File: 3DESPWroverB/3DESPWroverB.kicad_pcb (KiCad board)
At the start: 2 copper layers, 92.2 x 40 mm, 18 parts, among them J1 Conn_02x07_Odd_Even, J10 Conn_02x03_Odd_Even, J11 Conn_01x01, J12 Conn_01x01, J13 Conn_01x01, J14 Conn_01x01, J15 Conn_01x01, J16 Conn_01x01, J17 Conn_01x01, J18 Conn_01x01, J2 Conn_01x01, J3 Conn_01x01, J4 Conn_01x01, J5 Conn_01x01, J6 Conn_01x01, J7 Conn_01x01, J8 Conn_01x01, J9 Conn_01x01

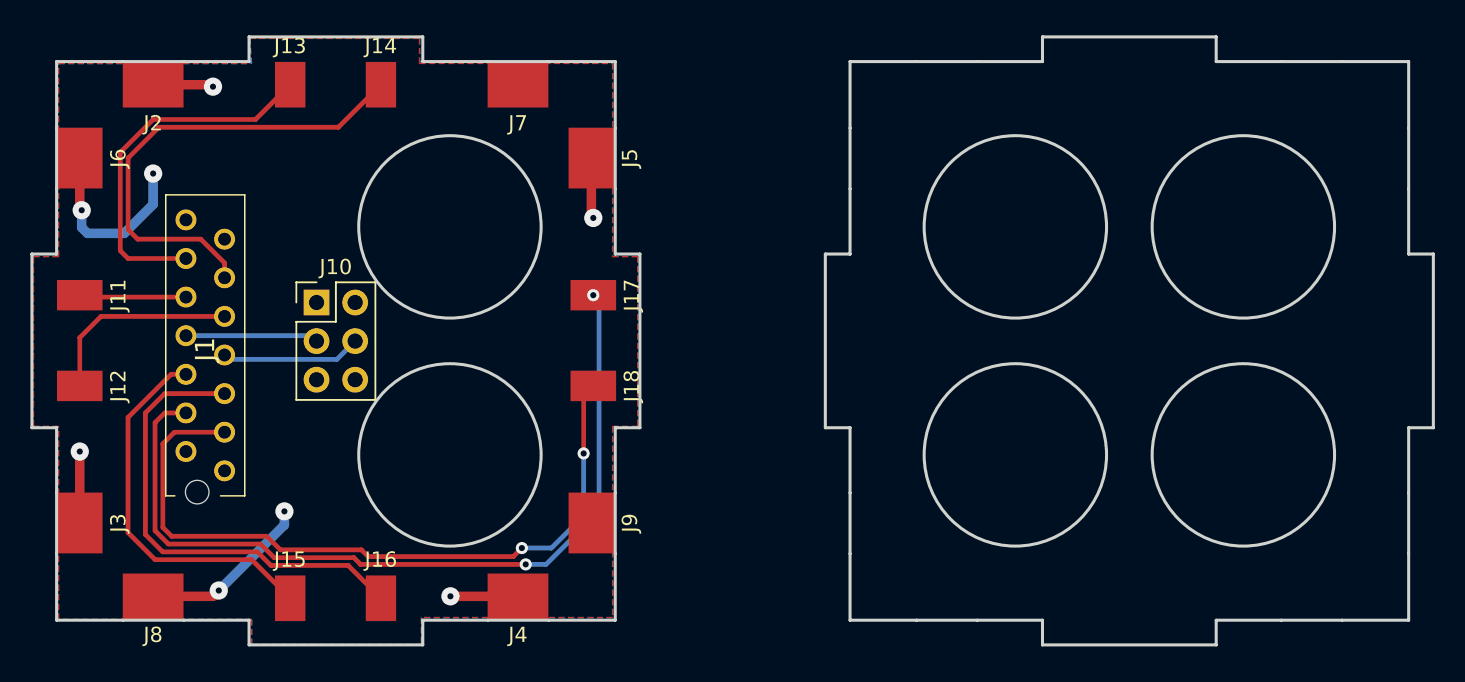
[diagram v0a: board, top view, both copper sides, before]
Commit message: Made corrections and added holes for zipties/nylon
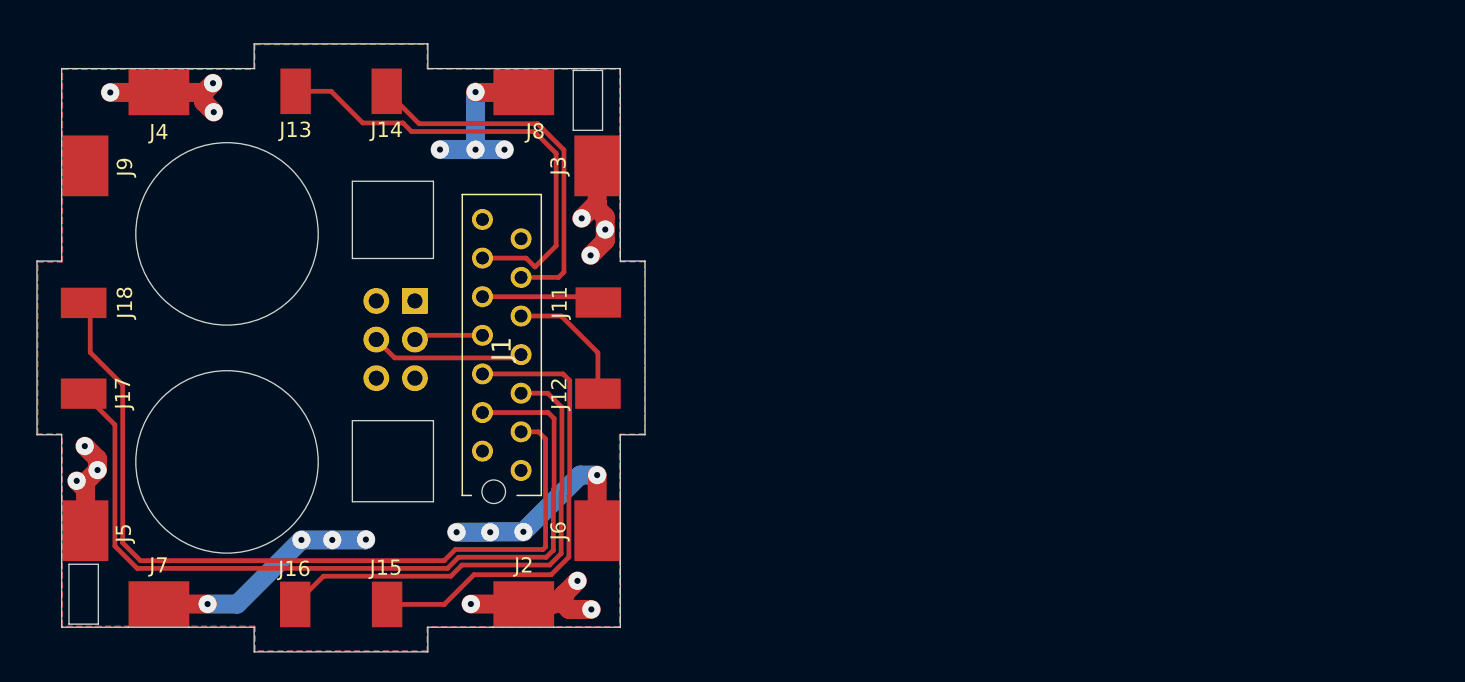
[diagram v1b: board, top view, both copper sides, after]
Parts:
- J10: moved to B.Cu
- moved J2 42.0 mm to (163.7, 74.3), turned to 180 degrees
- moved J6 41.9 mm to (168.5, 69.5), turned to 270 degrees
- moved J7 41.5 mm to (139.7, 74.3), turned to 180 degrees
- moved J3 41.4 mm to (168.5, 45.5), turned to 270 degrees
- moved J5 41.3 mm to (134.9, 69.5), turned to 270 degrees
- moved J8 41.1 mm to (163.7, 40.6), turned to 180 degrees
- moved J9 40.7 mm to (134.9, 45.5), turned to 270 degrees
- moved J4 40.7 mm to (139.7, 40.6), turned to 180 degrees
- moved J17 34.1 mm to (134.7, 60.5), turned to 270 degrees
- moved J11 34.1 mm to (168.6, 54.5), turned to 270 degrees
- moved J12 34.1 mm to (168.6, 60.5), turned to 270 degrees
- moved J18 34.0 mm to (134.7, 54.5), turned to 270 degrees
- moved J1 19.5 mm to (161.0, 49.0)
- moved J10 6.47 mm to (156.5, 54.4), turned to 180 degrees
- moved J15 6.39 mm to (154.7, 74.3), turned to 0 degrees
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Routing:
- net GND: track 23.8 -> 41.0 mm, vias 4 -> 12
- net VCC: track 17.1 -> 33.8 mm, vias 4 -> 12
- net /D8: track 31.6 -> 24.3 mm
- net /D7: track 24.0 -> 30.6 mm
- net /D13: track 25.0 -> 30.8 mm
- net /D16: track 48.8 -> 54.4 mm, vias 2 -> 0
- net /D11: track 9.24 -> 4.56 mm
- net /D10: track 13.3 -> 8.75 mm
- net /D15: track 55.4 -> 54.4 mm, vias 2 -> 0
- net /D9: track 7.04 -> 7.78 mm
- net /D14: track 31.0 -> 31.6 mm
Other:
- board size 92.2 x 40 mm -> 40 x 40 mm
- net class Power: trace_width 0.625 -> 1.25
- board text added: "Project Cube, v1.1"
- board text added: "REAL ITU rodr"
